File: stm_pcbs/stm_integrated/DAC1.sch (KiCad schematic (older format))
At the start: 21 parts, among them P2 BNC, U4 AD8676, U5 AD5791, U6 AD8675

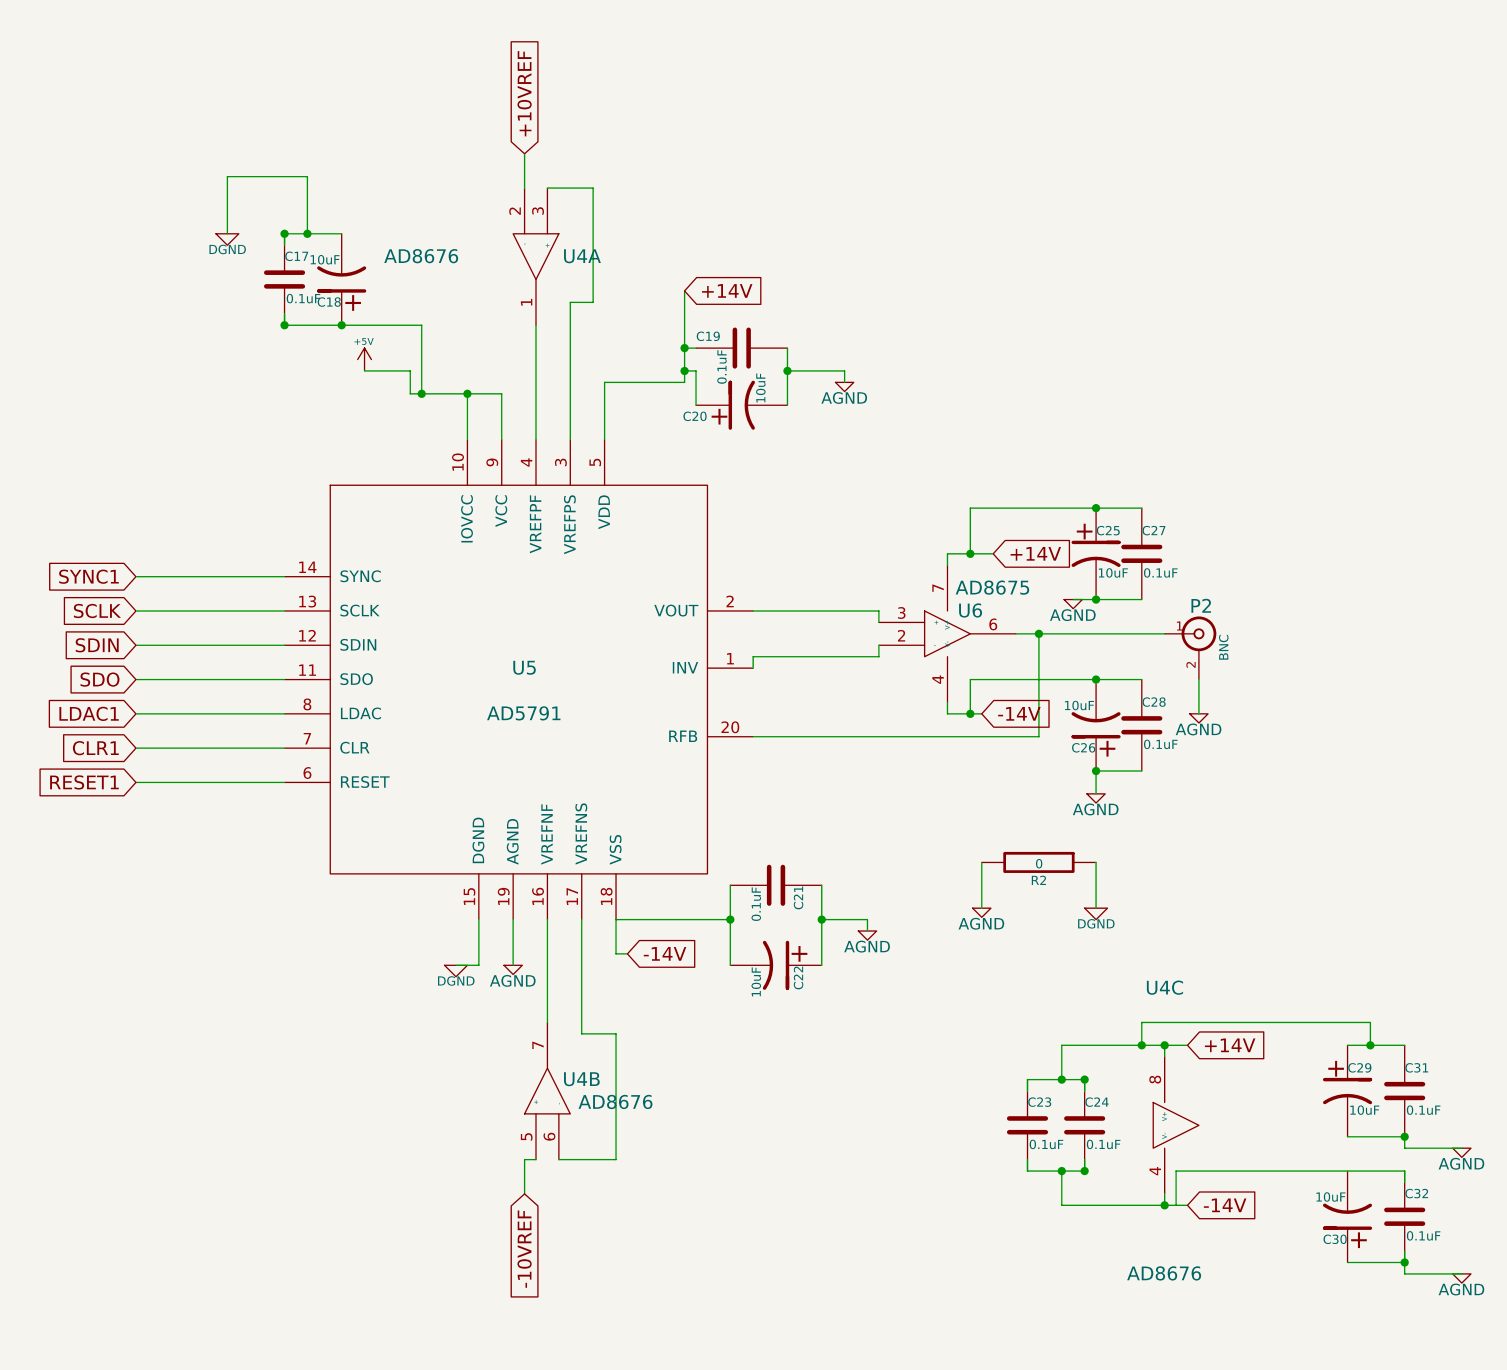
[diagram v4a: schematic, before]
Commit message: fixed issue with DAC (opamp wiring was wrong)
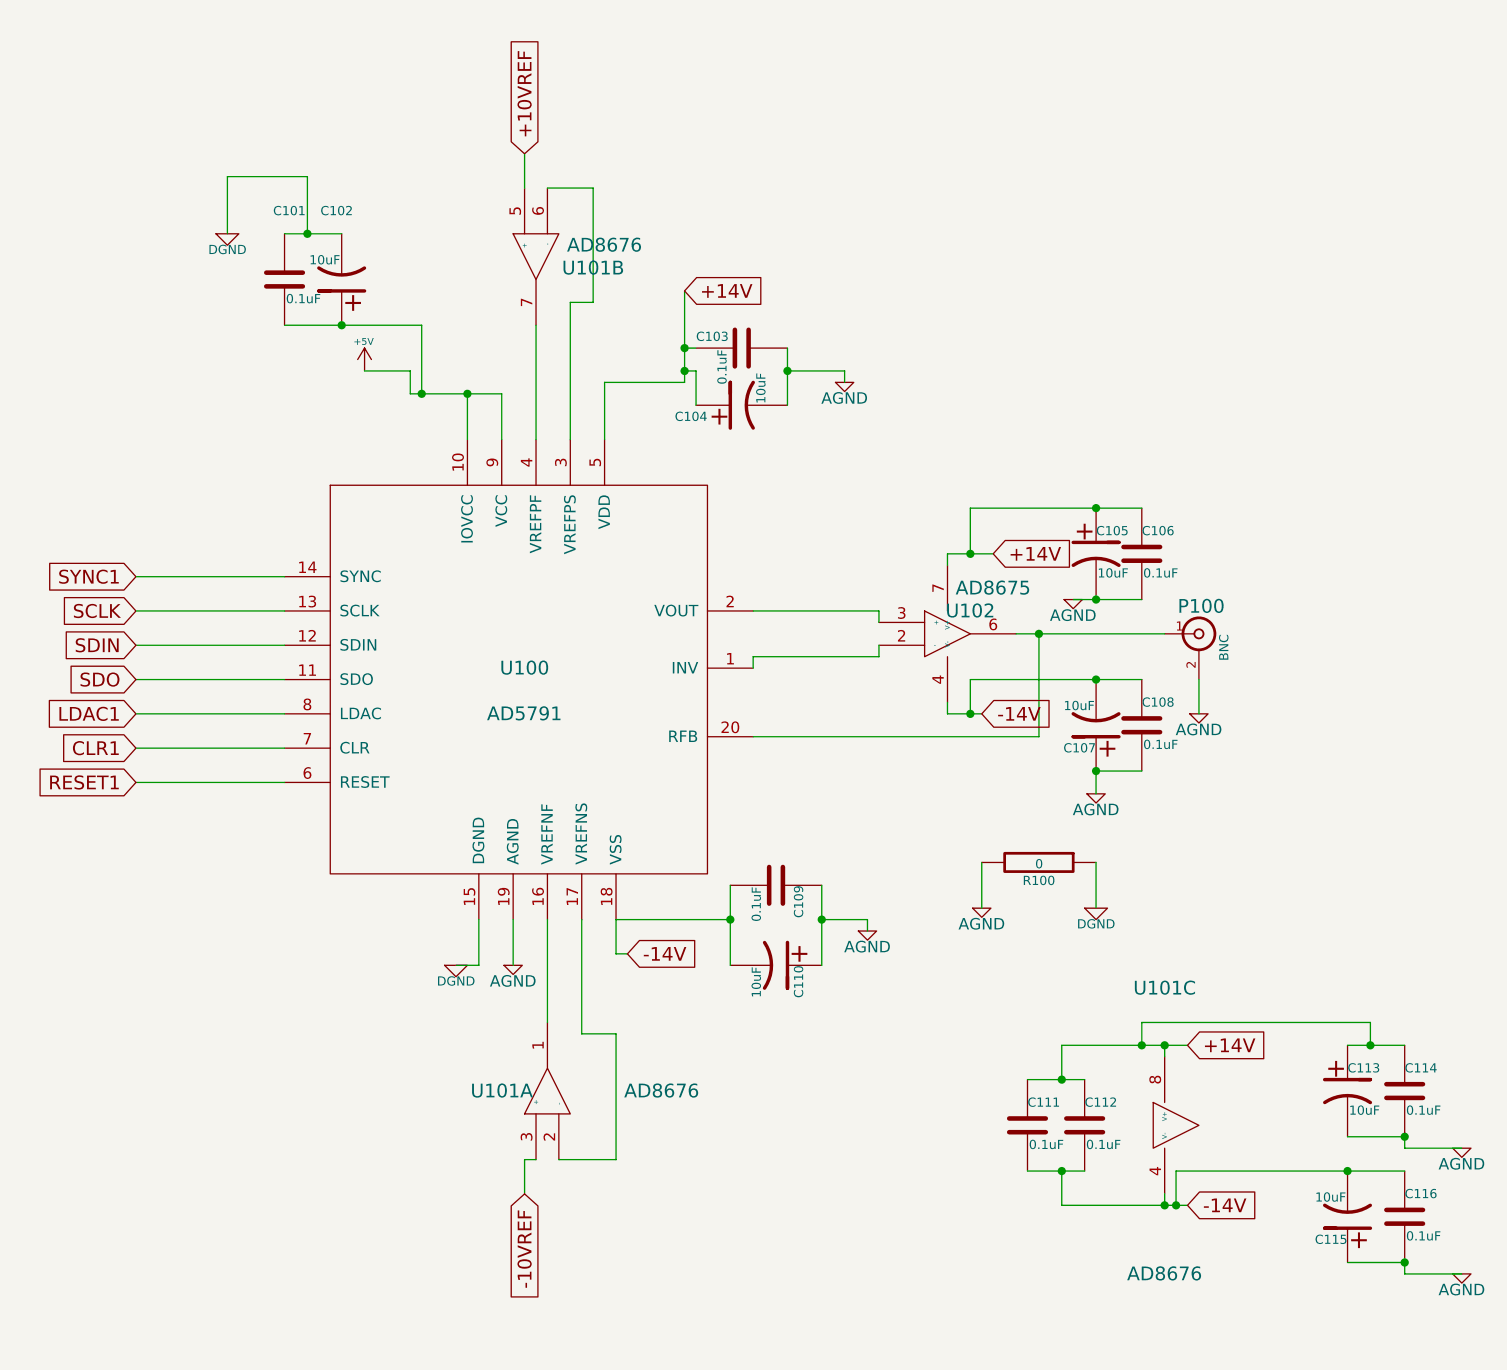
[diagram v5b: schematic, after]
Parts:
- renumbered P2 to P100, U5 to U100, U4 to U101, U6 to U102
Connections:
- wire segments 121 -> 115
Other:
- moved on the sheet: U101A, U101B
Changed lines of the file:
@@
 $EndDescr
 $Comp
-L ad5791:AD5791 U5
+L ad5791:AD5791 U100
 U 1 1 5A25DBB7
 P 5050 3900
-F 0 "U5" H 4900 4100 60  0000 C CNN
+F 0 "U100" H 4900 4100 60  0000 C CNN
 F 1 "AD5791" H 4900 3900 60  0000 C CNN
 F 2 "stm:SSOP-20" H 5050 3950 60  0001 C CNN
@@
 $EndComp
 $Comp
-L ad5791:AD8675 U6
+L ad5791:AD8675 U102
 U 1 1 5A25DBBE
 P 6750 3550
-F 0 "U6" H 6850 3650 60  0000 C CNN
+F 0 "U102" H 6850 3650 60  0000 C CNN
 F 1 "AD8675" H 6950 3750 60  0000 C CNN
 F 2 "stm:SOIC-8" H 6950 3500 60  0001 C CNN
@@
 $EndComp
 $Comp
-L ad5791:AD8676 U4
+L ad5791:AD8676 U101
 U 1 1 5A25DBC5
+P 5000 5600
+F 0 "U101" V 5050 5800 60  0000 C CNN
+F 1 "AD8676" V 5050 5100 60  0000 C CNN
+F 2 "stm:SOIC-8" H 5150 5600 60  0001 C CNN
+F 3 "" H 5150 5600 60  0000 C CNN
+	1    5000 5600
+	0    -1   -1   0
+$EndComp
+$Comp
+L ad5791:AD8676 U101
+U 2 1 5A25DBCC
 P 4950 1850
-F 0 "U4" V 5000 2050 60  0000 C CNN
-F 1 "AD8676" V 5000 1350 60  0000 C CNN
+F 0 "U101" V 5050 1600 60  0000 C CNN
+F 1 "AD8676" V 4950 1550 60  0000 C CNN
 F 2 "stm:SOIC-8" H 5100 1850 60  0001 C CNN
 F 3 "" H 5100 1850 60  0000 C CNN
-	1    4950 1850
-	0    1    1    0
-$EndComp
-$Comp
-L ad5791:AD8676 U4
-U 2 1 5A25DBCC
-P 5000 5600
-F 0 "U4" V 5100 5450 60  0000 C CNN
-F 1 "AD8676" V 5000 5300 60  0000 C CNN
-F 2 "stm:SOIC-8" H 5150 5600 60  0001 C CNN
-F 3 "" H 5150 5600 60  0000 C CNN
-	2    5000 5600
-	0    -1   -1   0
-$EndComp
-$Comp
-L ad5791:AD8676 U4
+	2    4950 1850
+	0    -1   1    0
+$EndComp
+$Comp
+L ad5791:AD8676 U101
 U 3 1 5A25DBD3
 P 7700 5700
-F 0 "U4" H 7700 6300 60  0000 C CNN
+F 0 "U101" H 7700 6300 60  0000 C CNN
 F 1 "AD8676" H 7700 5050 60  0000 C CNN
 F 2 "stm:SOIC-8" H 7850 5700 60  0001 C CNN
@@
 $EndComp
 $Comp
-L device:BNC P2
+L device:BNC P100
 U 1 1 5A25DBDA
 P 7850 3550
-F 0 "P2" H 7860 3670 60  0000 C CNN
+F 0 "P100" H 7860 3670 60  0000 C CNN
 F 1 "BNC" V 7960 3490 40  0000 C CNN
 F 2 "stm:SMA" H 7850 3550 60  0001 C CNN
@@
 P 5850 2300
 AR Path="/5A25DBFC" Ref="C19"  Part="1"
-AR Path="/5A25907D/5A25DBFC" Ref="C19"  Part="1"
-F 0 "C19" V 5800 2100 40  0000 L CNN
+AR Path="/5A25907D/5A25DBFC" Ref="C103"  Part="1"
+F 0 "C103" V 5800 2100 40  0000 L CNN
 F 1 "0.1uF" H 5856 2215 40  0000 L CNN
 F 2 "Capacitors_SMD:C_0805_HandSoldering" H 5888 2150 30  0001 C CNN
@@
 P 6000 4650
 AR Path="/5A25DC09" Ref="C21"  Part="1"
-AR Path="/5A25907D/5A25DC09" Ref="C21"  Part="1"
-F 0 "C21" H 6000 4750 40  0000 L CNN
+AR Path="/5A25907D/5A25DC09" Ref="C109"  Part="1"
+F 0 "C109" H 6000 4750 40  0000 L CNN
 F 1 "0.1uF" H 6006 4565 40  0000 L CNN
 F 2 "Capacitors_SMD:C_0805_HandSoldering" H 6038 4500 30  0001 C CNN
@@
 P 3850 2000
 AR Path="/5A25DC24" Ref="C17"  Part="1"
-AR Path="/5A25907D/5A25DC24" Ref="C17"  Part="1"
-F 0 "C17" H 3850 2100 40  0000 L CNN
+AR Path="/5A25907D/5A25DC24" Ref="C101"  Part="1"
+F 0 "C101" H 3800 2300 40  0000 L CNN
 F 1 "0.1uF" H 3856 1915 40  0000 L CNN
 F 2 "Capacitors_SMD:C_0805_HandSoldering" H 3888 1850 30  0001 C CNN
@@
 P 7350 5700
 AR Path="/5A25DC31" Ref="C24"  Part="1"
-AR Path="/5A25907D/5A25DC31" Ref="C24"  Part="1"
-F 0 "C24" H 7350 5800 40  0000 L CNN
+AR Path="/5A25907D/5A25DC31" Ref="C112"  Part="1"
+F 0 "C112" H 7350 5800 40  0000 L CNN
 F 1 "0.1uF" H 7356 5615 40  0000 L CNN
 F 2 "Capacitors_SMD:C_0805_HandSoldering" H 7388 5550 30  0001 C CNN
@@
 P 8750 5550
 AR Path="/5A25DC38" Ref="C31"  Part="1"
-AR Path="/5A25907D/5A25DC38" Ref="C31"  Part="1"
-F 0 "C31" H 8750 5650 40  0000 L CNN
+AR Path="/5A25907D/5A25DC38" Ref="C114"  Part="1"
+F 0 "C114" H 8750 5650 40  0000 L CNN
 F 1 "0.1uF" H 8756 5465 40  0000 L CNN
 F 2 "Capacitors_SMD:C_0805_HandSoldering" H 8788 5400 30  0001 C CNN
@@
 P 8750 6100
 AR Path="/5A25DC3F" Ref="C32"  Part="1"
-AR Path="/5A25907D/5A25DC3F" Ref="C32"  Part="1"
-F 0 "C32" H 8750 6200 40  0000 L CNN
+AR Path="/5A25907D/5A25DC3F" Ref="C116"  Part="1"
+F 0 "C116" H 8750 6200 40  0000 L CNN
 F 1 "0.1uF" H 8756 6015 40  0000 L CNN
 F 2 "Capacitors_SMD:C_0805_HandSoldering" H 8788 5950 30  0001 C CNN
@@
 P 7100 5700
 AR Path="/5A25DC52" Ref="C23"  Part="1"
-AR Path="/5A25907D/5A25DC52" Ref="C23"  Part="1"
-F 0 "C23" H 7100 5800 40  0000 L CNN
+AR Path="/5A25907D/5A25DC52" Ref="C111"  Part="1"
+F 0 "C111" H 7100 5800 40  0000 L CNN
 F 1 "0.1uF" H 7106 5615 40  0000 L CNN
 F 2 "Capacitors_SMD:C_0805_HandSoldering" H 7138 5550 30  0001 C CNN
@@
 P 8500 5550
 AR Path="/5A25DC59" Ref="C29"  Part="1"
-AR Path="/5A25907D/5A25DC59" Ref="C29"  Part="1"
-F 0 "C29" H 8500 5650 40  0000 L CNN
+AR Path="/5A25907D/5A25DC59" Ref="C113"  Part="1"
+F 0 "C113" H 8500 5650 40  0000 L CNN
 F 1 "10uF" H 8506 5465 40  0000 L CNN
 F 2 "stm:SMD-1210_Pol" H 8538 5400 30  0001 C CNN
@@
 P 8500 6100
 AR Path="/5A25DC60" Ref="C30"  Part="1"
-AR Path="/5A25907D/5A25DC60" Ref="C30"  Part="1"
-F 0 "C30" H 8500 6200 40  0000 L CNN
+AR Path="/5A25907D/5A25DC60" Ref="C115"  Part="1"
+F 0 "C115" H 8500 6200 40  0000 L CNN
 F 1 "10uF" H 8506 6015 40  0000 L CNN
 F 2 "stm:SMD-1210_Pol" H 8538 5950 30  0001 C CNN
@@
 P 6000 5000
 AR Path="/5A25DC67" Ref="C22"  Part="1"
-AR Path="/5A25907D/5A25DC67" Ref="C22"  Part="1"
-F 0 "C22" H 6000 5100 40  0000 L CNN
+AR Path="/5A25907D/5A25DC67" Ref="C110"  Part="1"
+F 0 "C110" H 6000 5100 40  0000 L CNN
 F 1 "10uF" H 6006 4915 40  0000 L CNN
 F 2 "stm:SMD-1210_Pol" H 6038 4850 30  0001 C CNN
@@
 P 5850 2550
 AR Path="/5A25DC6E" Ref="C20"  Part="1"
-AR Path="/5A25907D/5A25DC6E" Ref="C20"  Part="1"
-F 0 "C20" V 5800 2700 40  0000 L CNN
+AR Path="/5A25907D/5A25DC6E" Ref="C104"  Part="1"
+F 0 "C104" V 5800 2700 40  0000 L CNN
 F 1 "10uF" H 5856 2465 40  0000 L CNN
 F 2 "stm:SMD-1210_Pol" H 5888 2400 30  0001 C CNN
@@
 P 4100 2000
 AR Path="/5A25DC75" Ref="C18"  Part="1"
-AR Path="/5A25907D/5A25DC75" Ref="C18"  Part="1"
-F 0 "C18" H 4100 2100 40  0000 L CNN
+AR Path="/5A25907D/5A25DC75" Ref="C102"  Part="1"
+F 0 "C102" H 4050 1700 40  0000 L CNN
 F 1 "10uF" H 4106 1915 40  0000 L CNN
 F 2 "stm:SMD-1210_Pol" H 4138 1850 30  0001 C CNN
@@
 P 7400 3200
 AR Path="/5A25DC83" Ref="C25"  Part="1"
-AR Path="/5A25907D/5A25DC83" Ref="C25"  Part="1"
-F 0 "C25" H 7400 3300 40  0000 L CNN
+AR Path="/5A25907D/5A25DC83" Ref="C105"  Part="1"
+F 0 "C105" H 7400 3300 40  0000 L CNN
 F 1 "10uF" H 7406 3115 40  0000 L CNN
 F 2 "stm:SMD-1210_Pol" H 7438 3050 30  0001 C CNN
@@
 P 7400 3950
 AR Path="/5A25DC8A" Ref="C26"  Part="1"
-AR Path="/5A25907D/5A25DC8A" Ref="C26"  Part="1"
-F 0 "C26" H 7400 4050 40  0000 L CNN
+AR Path="/5A25907D/5A25DC8A" Ref="C107"  Part="1"
+F 0 "C107" H 7400 4050 40  0000 L CNN
 F 1 "10uF" H 7406 3865 40  0000 L CNN
 F 2 "stm:SMD-1210_Pol" H 7438 3800 30  0001 C CNN
@@
 P 7600 3200
 AR Path="/5A25DC91" Ref="C27"  Part="1"
-AR Path="/5A25907D/5A25DC91" Ref="C27"  Part="1"
-F 0 "C27" H 7600 3300 40  0000 L CNN
+AR Path="/5A25907D/5A25DC91" Ref="C106"  Part="1"
+F 0 "C106" H 7600 3300 40  0000 L CNN
 F 1 "0.1uF" H 7606 3115 40  0000 L CNN
 F 2 "Capacitors_SMD:C_0805_HandSoldering" H 7638 3050 30  0001 C CNN
@@
 P 7600 3950
 AR Path="/5A25DC98" Ref="C28"  Part="1"
-AR Path="/5A25907D/5A25DC98" Ref="C28"  Part="1"
-F 0 "C28" H 7600 4050 40  0000 L CNN
+AR Path="/5A25907D/5A25DC98" Ref="C108"  Part="1"
+F 0 "C108" H 7600 4050 40  0000 L CNN
 F 1 "0.1uF" H 7606 3865 40  0000 L CNN
 F 2 "Capacitors_SMD:C_0805_HandSoldering" H 7638 3800 30  0001 C CNN
@@
 	8750 6350 9000 6350
 Wire Wire Line
-	8750 6250 8750 6300
-Wire Wire Line
 	3200 4200 3850 4200
 Wire Wire Line
@@
 P 7150 4550
 AR Path="/5A25DD1F" Ref="R2"  Part="1"
-AR Path="/5A25907D/5A25DD1F" Ref="R2"  Part="1"
-F 0 "R2" V 7230 4550 40  0000 C CNN
+AR Path="/5A25907D/5A25DD1F" Ref="R100"  Part="1"
+F 0 "R100" V 7230 4550 40  0000 C CNN
 F 1 "0" V 7157 4551 40  0000 C CNN
 F 2 "stm:0Ohm" V 7080 4550 30  0001 C CNN
@@
 $EndComp
 Wire Wire Line
-	3850 2150 3850 2200
-Wire Wire Line
-	3850 1850 3850 1800
-Wire Wire Line
 	3200 3300 3850 3300
 Wire Wire Line
 	7400 4250 7400 4150
-Wire Wire Line
-	7350 5500 7350 5550
-Wire Wire Line
-	7350 5900 7350 5850
-Wire Wire Line
-	7100 5900 7100 5850
-Wire Wire Line
-	7100 5550 7100 5500
-Wire Wire Line
-	8750 5900 8750 5950
 Connection ~ 8750 6300
 Connection ~ 8750 5750
@@
 	7250 6050 7700 6050
 Wire Wire Line
-	7700 6050 7800 6050
-Wire Wire Line
 	6850 3000 7400 3000
 Wire Wire Line
 	6850 3750 7400 3750
-Wire Wire Line
-	7750 5900 8750 5900
 Wire Wire Line
 	7300 3400 7400 3400
@@
 Wire Wire Line
 	4100 2200 4450 2200
-Connection ~ 3850 1800
-Connection ~ 3850 2200
-Connection ~ 7350 5500
-Connection ~ 7350 5900
 $Comp
 L power:+5V #PWR080
@@
 Wire Wire Line
 	4200 2400 4400 2400
+Wire Wire Line
+	7750 5900 8500 5900
+Connection ~ 8500 5900
+Wire Wire Line
+	8500 5900 8750 5900
+Wire Wire Line
+	7700 6050 7750 6050
+Connection ~ 7750 6050
+Wire Wire Line
+	7750 6050 7800 6050
 $EndSCHEMATC
